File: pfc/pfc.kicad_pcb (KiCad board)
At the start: 2 copper layers, 94 x 46 mm, 56 parts, among them J1 Conn_01x03_Male, J2 CONN_01X02, U1 NFET, U2 NFET, U3 BD7692FJ, U4 LNK304D

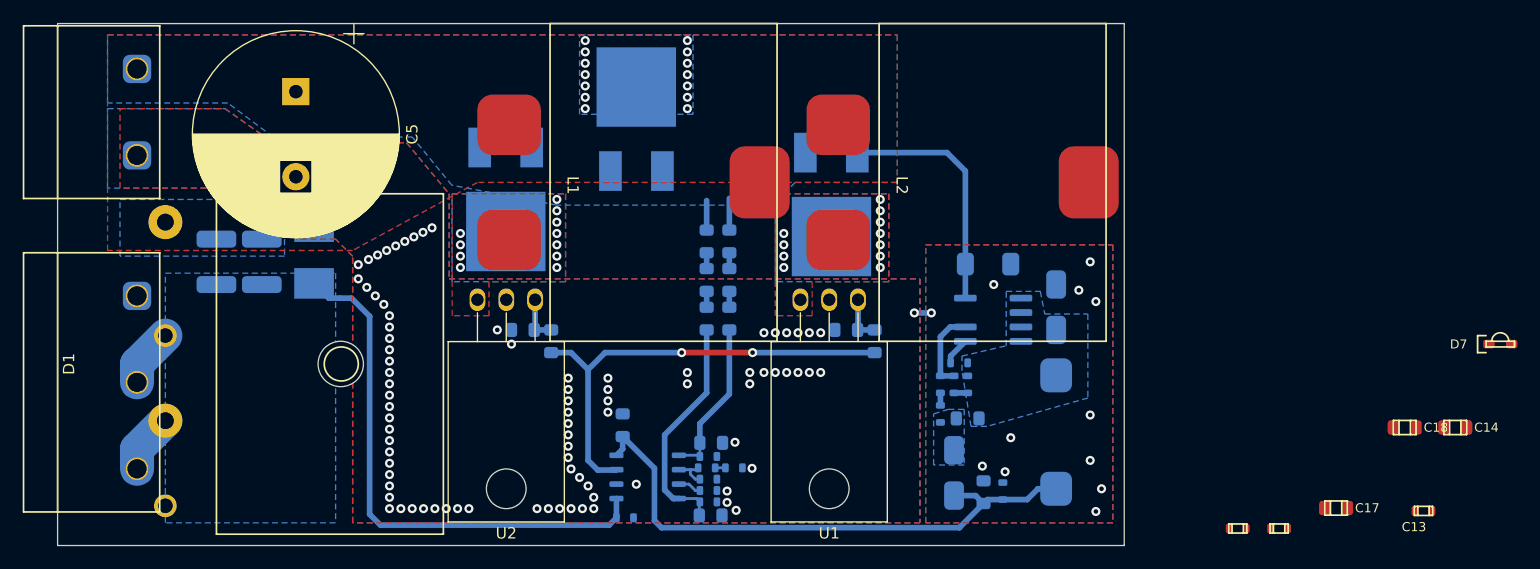
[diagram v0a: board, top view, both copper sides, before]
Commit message: add component values and mounting hole
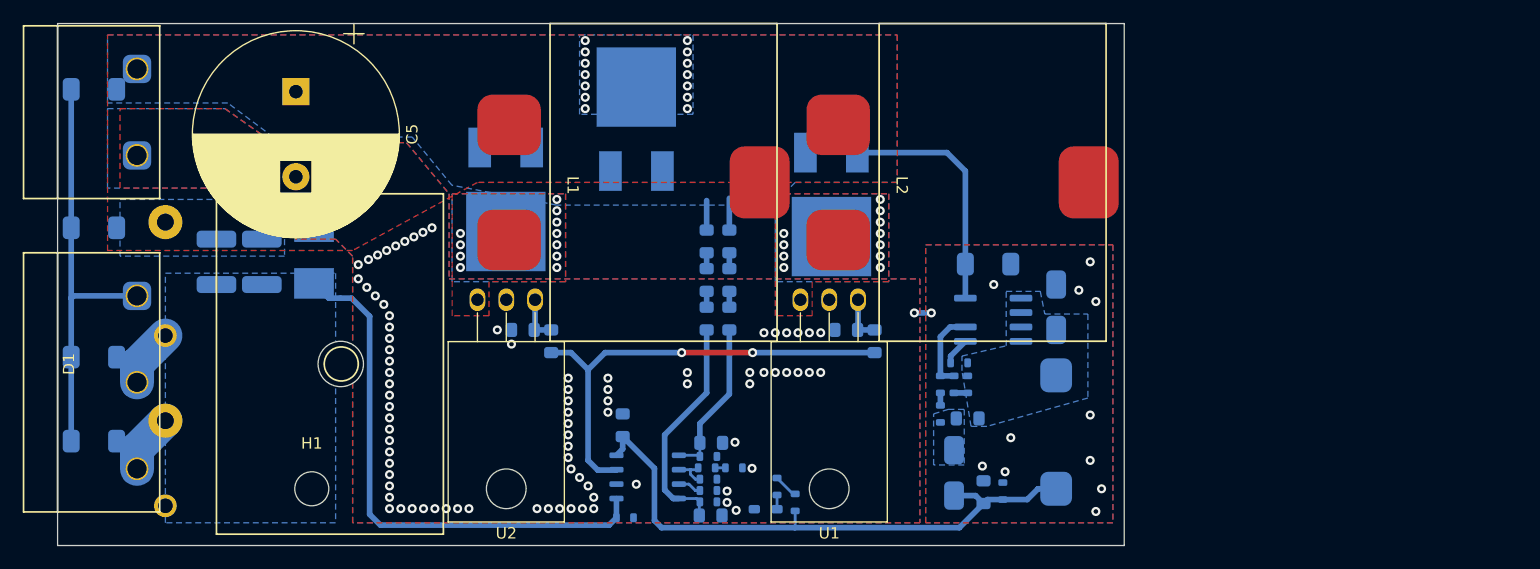
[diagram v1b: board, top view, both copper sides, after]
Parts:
- removed C13: 100n, stmbl:C_0603
- removed C14, C17, C18: 10µ, stmbl:C_0805
- added C19: C, stmbl-kicad-lib:C_1808, B.Cu at (49.2, 129.4)
- added C20: C, stmbl-kicad-lib:C_1808, B.Cu at (49.2, 136.8)
- added C21: C, stmbl-kicad-lib:C_1808, B.Cu at (49.2, 118.0)
- added C22: C, stmbl-kicad-lib:C_1808, B.Cu at (49.2, 105.8)
- added H1: MountingHole, MountingHole:MountingHole_3mm, F.Cu at (68.4, 141.0)
- C3, C4, C9: value C -> 1n
- D2, D3, D4: value D -> STPSC6H065B
- D7, R21, R22: moved to B.Cu
- R1: value R -> .06
- R10, R14: value R -> 390k
- R11, R15, R3, R5: value R -> 10k
- R12, R13, R8, R9: value R -> 500k
- R2, R4: value R -> 22
- R7: value R -> 39k
- moved D7 66.4 mm to (108.4, 142.8)
- moved R22 44.4 mm to (109.4, 140.8), turned to -90 degrees
- moved R21 39.1 mm to (111.0, 142.2), turned to 90 degrees
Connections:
- D2 pad : VPP -> (no net)
- D3 pad : VPP -> (no net)
- D4 pad : VPP -> (no net)
- J1 pad 1: Net-(J1-Pad1) -> Earth_Protective
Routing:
- net Earth_Protective: track 0.00 -> 36.9 mm
- net Net-(R21-Pad2): track 0.00 -> 2.18 mm
- net +15V: track 50.4 -> 51.9 mm
- net Net-(D7-Pad2): track 0.00 -> 1.25 mm
